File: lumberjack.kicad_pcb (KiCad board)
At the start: 2 copper layers, 285.4 x 94.9 mm, 151 parts, among them J1 USB_OTG, J2 AVR_ISP_6, SW1 RESET, SW2 BOOT, U1 ATMEGA328-PU, Y1 16MHz

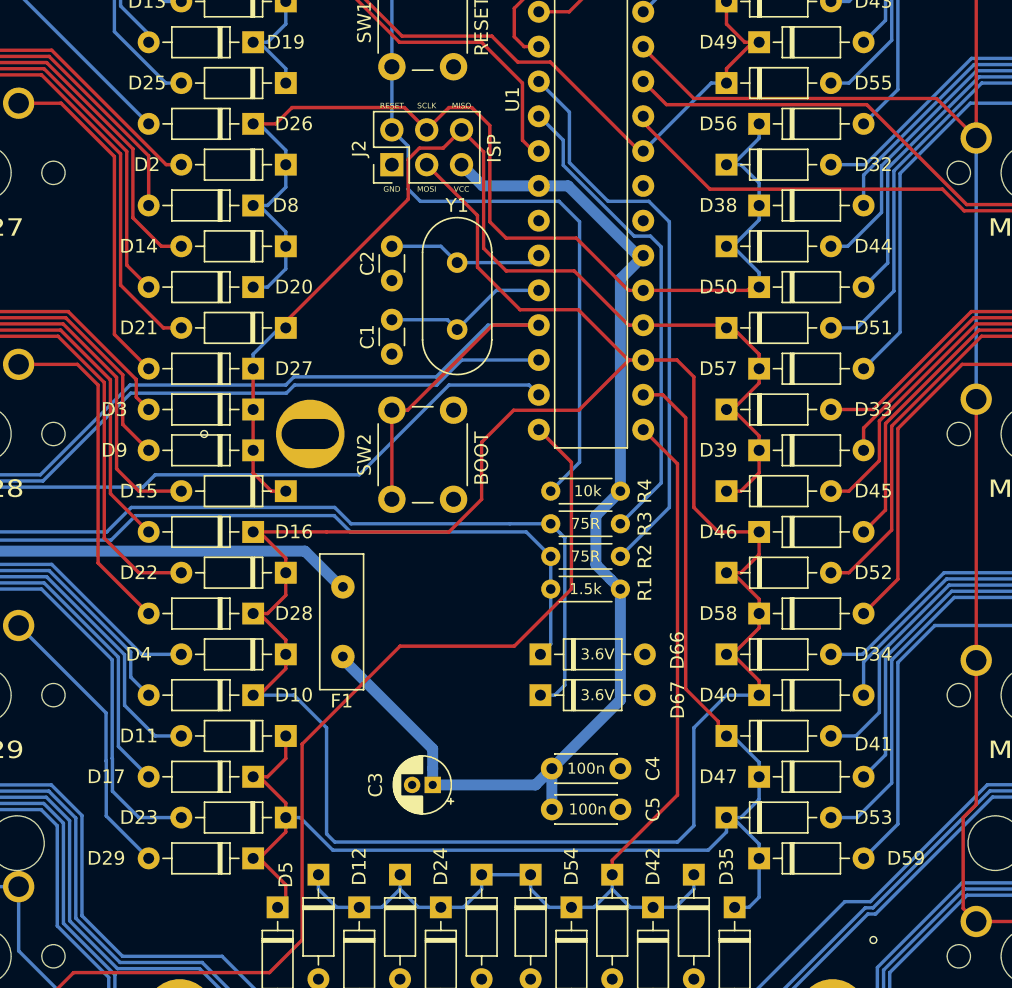
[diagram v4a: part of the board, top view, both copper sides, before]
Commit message: Fix cosmetic errors in silkscreen
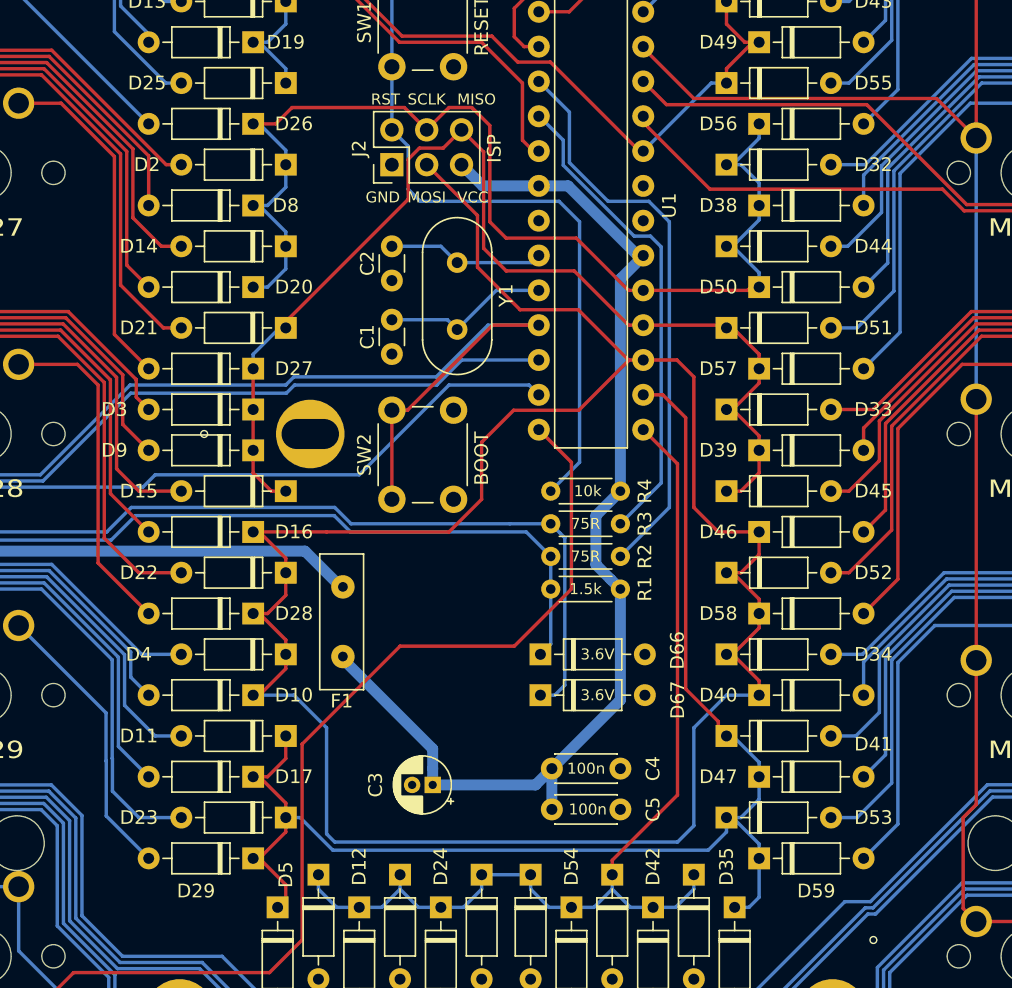
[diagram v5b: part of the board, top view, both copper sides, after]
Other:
- board text added: "RST"
- board text removed: "RESET"
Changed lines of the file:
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@@
   (general
     (thickness 1.6)
-    (drawings 140)
+    (drawings 141)
     (tracks 817)
     (zones 0)
@@
     (descr "Crystal THT HC-49-4H http://5hertz.com/pdfs/04404_D.pdf")
     (tags "THT crystalHC-49-4H")
-    (fp_text reference Y1 (at -4.167191 0 180) (layer F.SilkS)
+    (fp_text reference Y1 (at 2.381252 -3.571878 270) (layer F.SilkS)
       (effects (font (size 1 1) (thickness 0.15)))
     )
@@
     (descr "28-lead though-hole mounted DIP package, row spacing 7.62 mm (300 mils)")
     (tags "THT DIP DIL PDIP 2.54mm 7.62mm 300mil")
-    (fp_text reference U1 (at -1.905008 8.929695 90) (layer F.SilkS)
+    (fp_text reference U1 (at 9.525008 16.668764 90) (layer F.SilkS)
       (effects (font (size 1 1) (thickness 0.15)))
     )
@@
     (descr "Diode, DO-35_SOD27 series, Axial, Horizontal, pin pitch=7.62mm, , length*diameter=4*2mm^2, , http://www.diodes.com/_files/packages/DO-35.pdf")
     (tags "Diode DO-35_SOD27 series Axial Horizontal pin pitch 7.62mm  length 4mm diameter 2mm")
-    (fp_text reference D17 (at 10.715634 0) (layer F.SilkS)
+    (fp_text reference D17 (at -2.976565 0) (layer F.SilkS)
       (effects (font (size 1 1) (thickness 0.15)))
     )
@@
     (descr "Diode, DO-35_SOD27 series, Axial, Horizontal, pin pitch=7.62mm, , length*diameter=4*2mm^2, , http://www.diodes.com/_files/packages/DO-35.pdf")
     (tags "Diode DO-35_SOD27 series Axial Horizontal pin pitch 7.62mm  length 4mm diameter 2mm")
-    (fp_text reference D29 (at 10.715634 0) (layer F.SilkS)
+    (fp_text reference D29 (at 4.167191 -2.381252) (layer F.SilkS)
       (effects (font (size 1 1) (thickness 0.15)))
     )
@@
     (descr "Diode, DO-35_SOD27 series, Axial, Horizontal, pin pitch=7.62mm, , length*diameter=4*2mm^2, , http://www.diodes.com/_files/packages/DO-35.pdf")
     (tags "Diode DO-35_SOD27 series Axial Horizontal pin pitch 7.62mm  length 4mm diameter 2mm")
-    (fp_text reference D59 (at 10.715634 0) (layer F.SilkS)
+    (fp_text reference D59 (at 4.167191 2.381252) (layer F.SilkS)
       (effects (font (size 1 1) (thickness 0.15)))
     )
@@
       (net 92 "Net-(2u_MX60-Pad1)"))
   )
+  (dimension 4.762504 (width 0.15) (layer Eco2.User)
+    (gr_text "4.763 mm" (at 178.5939 153.104815) (layer Eco2.User)
+      (effects (font (size 1 1) (thickness 0.15)))
+    )
+    (feature1 (pts (xy 180.975152 144.661059) (xy 180.975152 152.391236)))
+    (feature2 (pts (xy 176.212648 144.661059) (xy 176.212648 152.391236)))
+    (crossbar (pts (xy 176.212648 151.804815) (xy 180.975152 151.804815)))
+    (arrow1a (pts (xy 180.975152 151.804815) (xy 179.848648 152.391236)))
+    (arrow1b (pts (xy 180.975152 151.804815) (xy 179.848648 151.218394)))
+    (arrow2a (pts (xy 176.212648 151.804815) (xy 177.339152 152.391236)))
+    (arrow2b (pts (xy 176.212648 151.804815) (xy 177.339152 151.218394)))
+  )
   (gr_line (start 152.400128 149.423563) (end 152.400128 51.196918) (layer Eco2.User) (width 0.15))
   (dimension 28.575024 (width 0.15) (layer Eco2.User)
@@
     (arrow2b (pts (xy 123.825104 154.78138) (xy 124.951608 154.194959)))
   )
-  (gr_text MISO (at 149.145746 78.45) (layer F.SilkS)
-    (effects (font (size 0.4 0.4) (thickness 0.1)))
+  (gr_text MISO (at 148.82825 77.986003) (layer F.SilkS)
+    (effects (font (size 0.8 0.8) (thickness 0.1)) (justify left))
   )
-  (gr_text SCLK (at 146.605746 78.45) (layer F.SilkS)
-    (effects (font (size 0.4 0.4) (thickness 0.1)))
+  (gr_text SCLK (at 146.605746 77.986003) (layer F.SilkS)
+    (effects (font (size 0.8 0.8) (thickness 0.1)))
   )
-  (gr_text MOSI (at 146.605746 84.534446) (layer F.SilkS)
-    (effects (font (size 0.4 0.4) (thickness 0.1)))
+  (gr_text MOSI (at 146.605746 85.129759) (layer F.SilkS)
+    (effects (font (size 0.8 0.8) (thickness 0.1)))
   )
-  (gr_text VCC (at 149.145746 84.534446) (layer F.SilkS)
-    (effects (font (size 0.4 0.4) (thickness 0.1)))
+  (gr_text VCC (at 148.82825 85.129759) (layer F.SilkS)
+    (effects (font (size 0.8 0.8) (thickness 0.1)) (justify left))
   )
-  (gr_text GND (at 144.07 84.534446) (layer F.SilkS)
-    (effects (font (size 0.4 0.4) (thickness 0.1)))
+  (gr_text GND (at 144.661059 85.129759) (layer F.SilkS)
+    (effects (font (size 0.8 0.8) (thickness 0.1)) (justify right))
   )
-  (gr_text RESET (at 144.07 78.45) (layer F.SilkS)
-    (effects (font (size 0.4 0.4) (thickness 0.1)))
+  (gr_text RST (at 144.661059 77.986003) (layer F.SilkS)
+    (effects (font (size 0.8 0.8) (thickness 0.1)) (justify right))
   )
   (gr_text ISP (at 151.537087 81.570333 90) (layer F.SilkS)

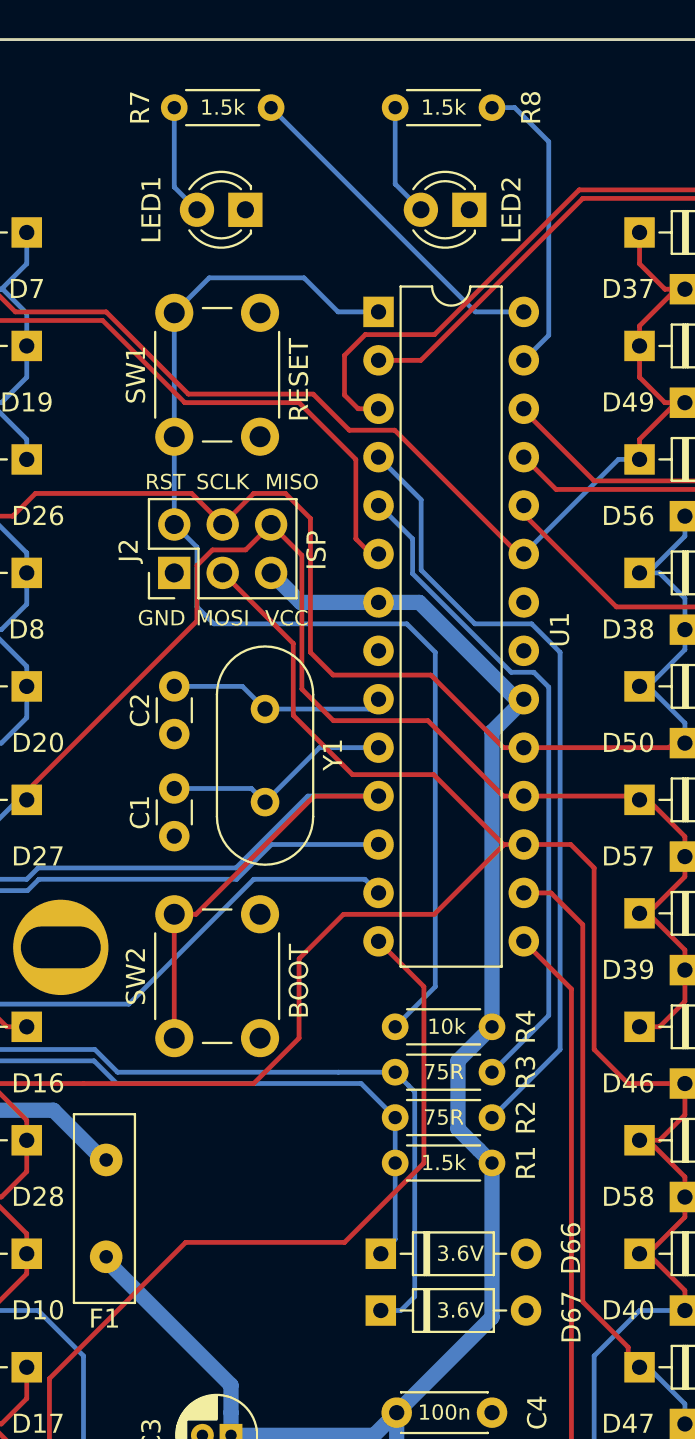
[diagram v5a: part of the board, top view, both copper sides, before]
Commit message: Increase resistor footprint size
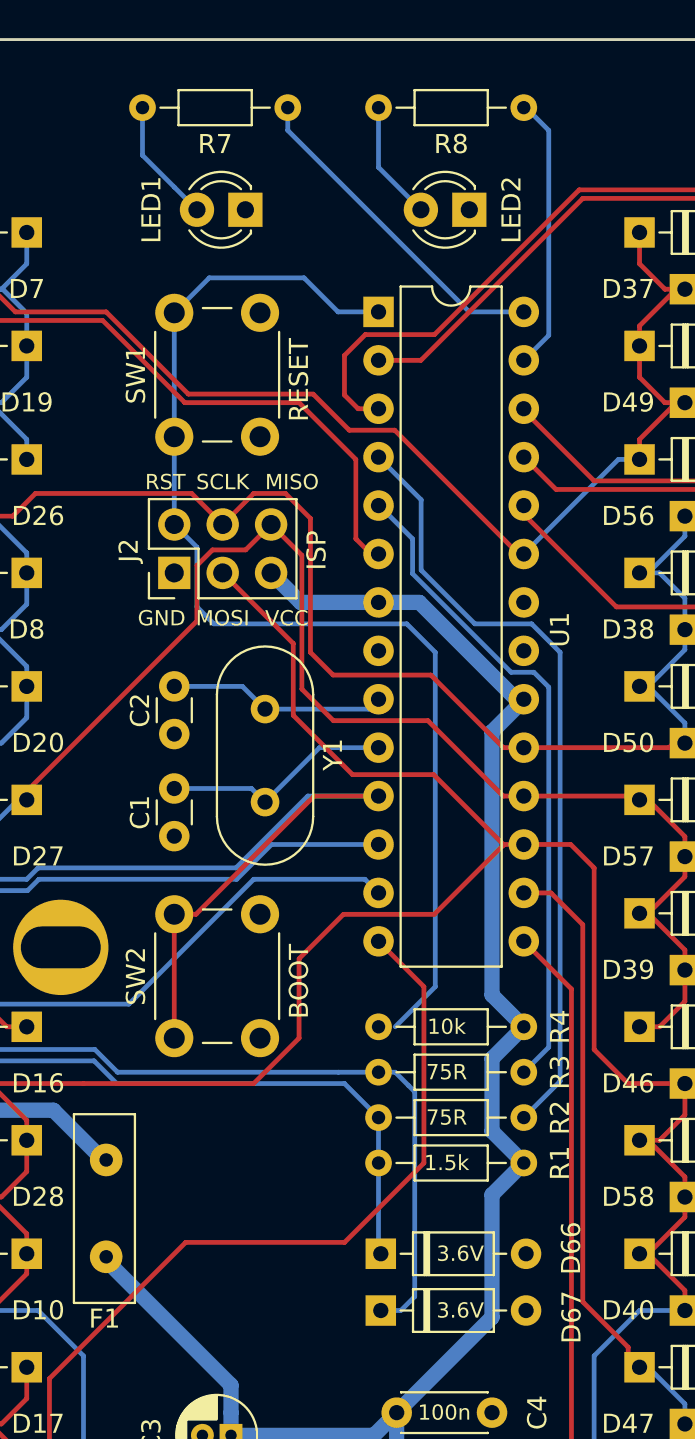
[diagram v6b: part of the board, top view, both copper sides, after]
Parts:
- R1, R2, R3, R4, R7, R8: footprint Resistor_THT:R_Axial_DIN0204_L3.6mm_D1.6mm_P5.08mm_Horizontal -> Resistor_THT:R_Axial_DIN0204_L3.6mm_D1.6mm_P7.62mm_Horizontal
- moved R2 1.67 mm to (162.4, 111.3)
- moved R3 1.67 mm to (162.4, 108.9)
- moved R4 1.67 mm to (162.4, 106.6)
- moved R8 1.67 mm to (162.4, 58.3)
- moved R7 0.87 mm to (150.0, 58.3)
- moved R1 0.87 mm to (154.8, 113.7)
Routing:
- net /LED2: track 15.7 -> 14.4 mm
- net +5V: track 81.7 -> 83.0 mm
- net Net-(D66-Pad1): track 182.1 -> 180.9 mm
- net /USB_D-: track 35.4 -> 34.7 mm
- net /USB_D+: track 41.8 -> 41.1 mm
- net Net-(LED1-Pad2): track 5.85 -> 6.54 mm

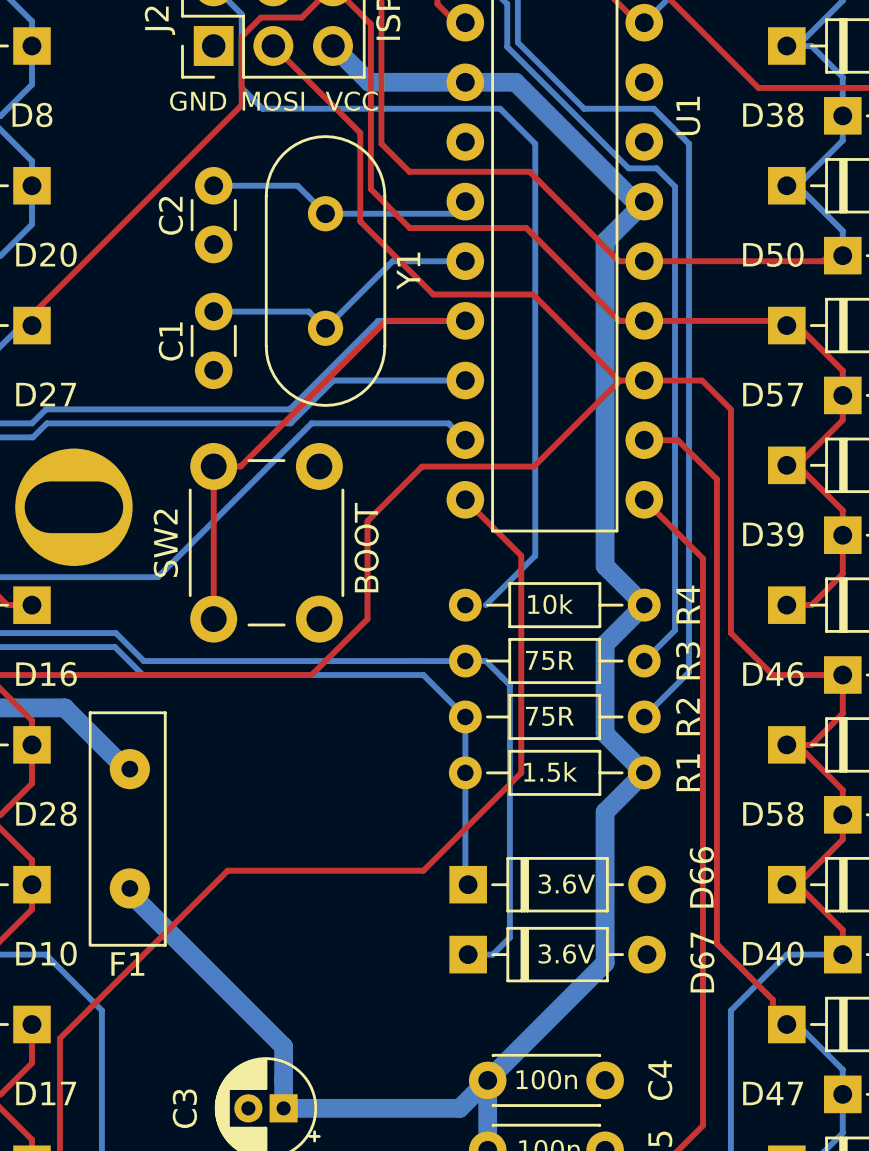
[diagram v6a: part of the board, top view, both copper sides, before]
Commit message: Fix R1 resistor connection to D-
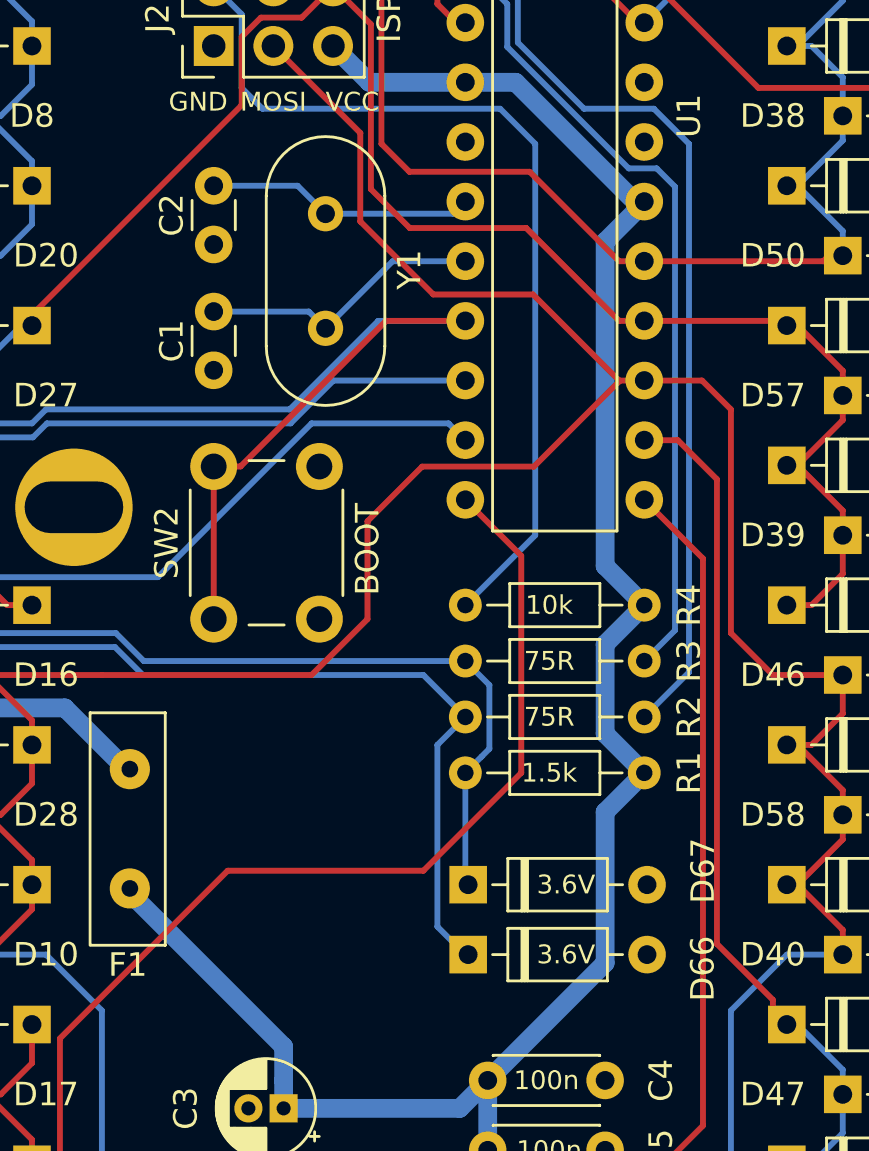
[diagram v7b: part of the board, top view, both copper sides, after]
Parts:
- moved D66 2.98 mm to (154.9, 121.4)
- moved D67 2.98 mm to (154.9, 118.5)
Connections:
- R1 pad 1: Net-(D66-Pad1) -> Net-(D67-Pad1)
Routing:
- net Net-(D67-Pad1): track 193.3 -> 188.6 mm
- net Net-(D66-Pad1): track 180.9 -> 185.0 mm
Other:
- board text added: "Lumberjack rev1.1 u/peejeh 12/2020"
- board text removed: "Lumberjack rev1 u/peejeh 10/2020"
